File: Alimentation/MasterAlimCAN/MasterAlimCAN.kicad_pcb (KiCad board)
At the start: 2 copper layers, 85 x 111 mm, 95 parts, among them J1 BATT, J10 Alim OUT, J11 ALIM 3 IN, J2 DEBUG, J3 In App Prog, J4 I2C1_5, J5 I2C2_5, J6 CAN1, J7 CAN2, J8 Conn AU, J9 Conn AU, Q1 BSS138, Q2 BSS138, SW1 RESET, SW2 BOOT0, U1 AMS1117-3.3, U10 PTN78020W_EUK-7, U2 STM32G474RETx, U3 74LVC1G02, U4 74LVC1G02, U5 MCP2558FD-xSN, U6 ACS711xEXLT-15AB, U7 ACS711xEXLT-15AB, U8 ACS711xEXLT-15AB, U9 PTN78020W_EUK-7, Y1 16MHz

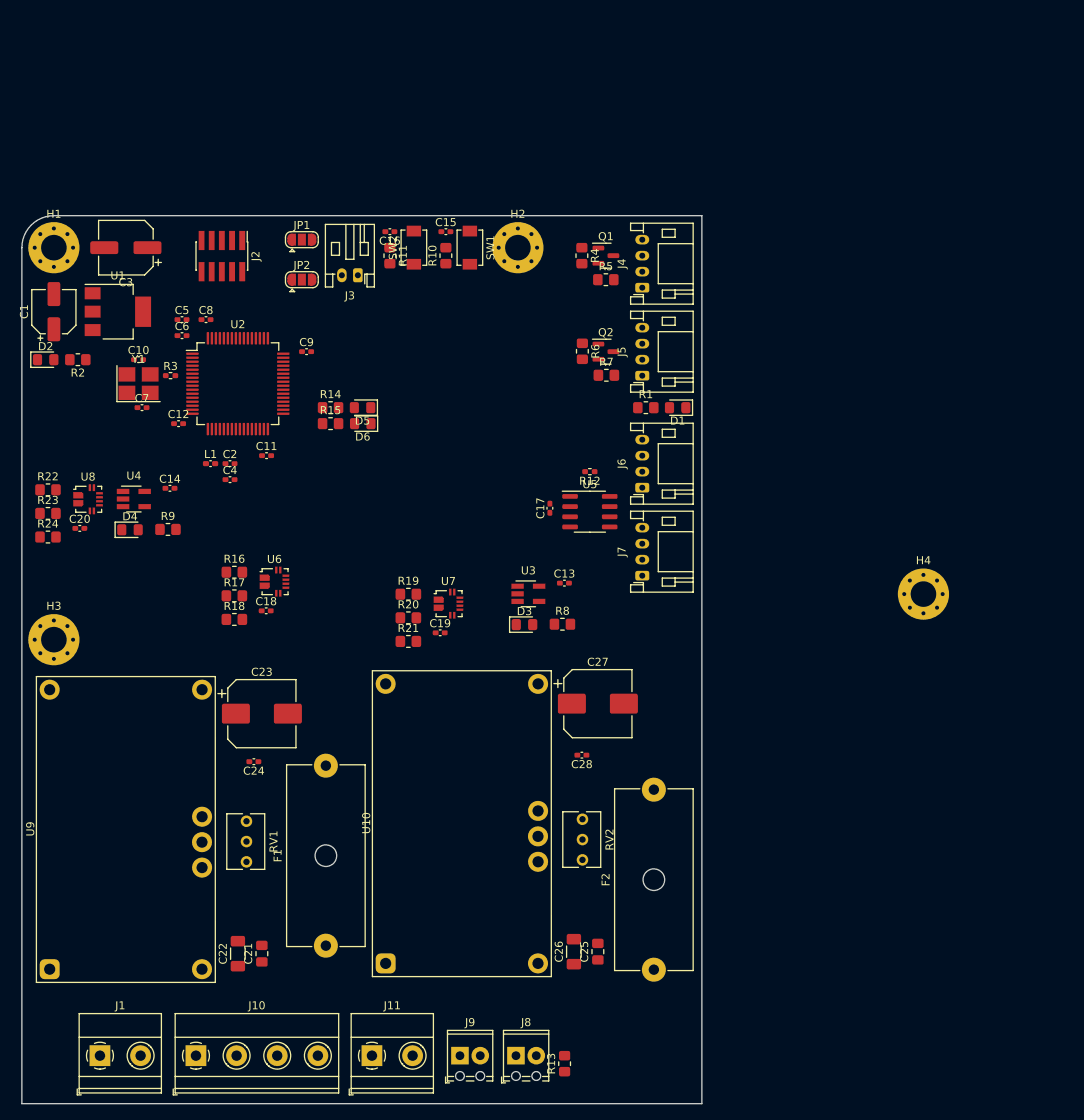
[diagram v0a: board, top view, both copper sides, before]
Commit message: New disposition for alim CAN
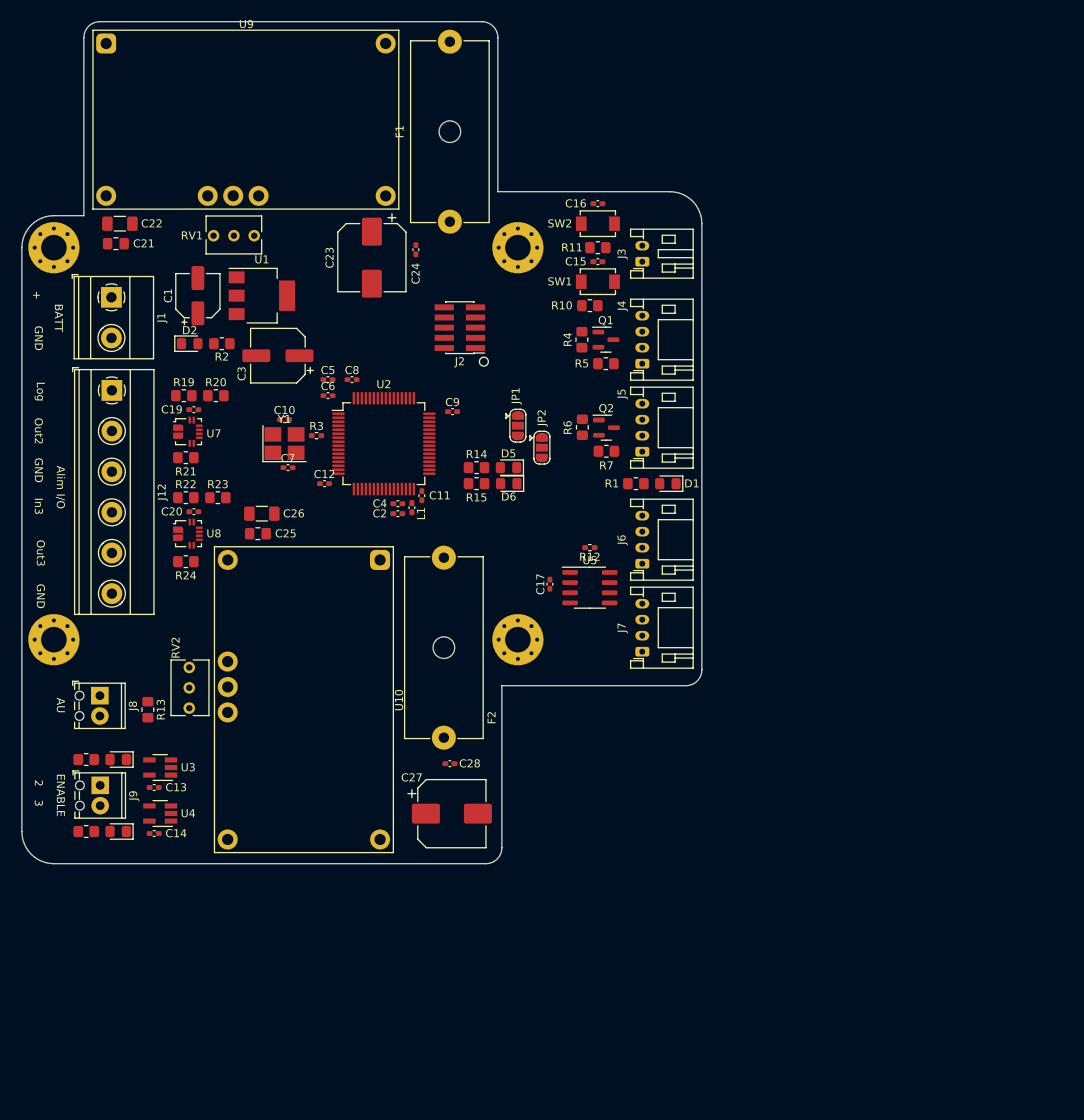
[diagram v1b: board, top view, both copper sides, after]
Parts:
- removed C18: 100n, Capacitor_SMD:C_0402_1005Metric_Pad0.74x0.62mm_HandSolder
- removed J10: Alim OUT, TerminalBlock_Phoenix:TerminalBlock_Phoenix_MKDS-1,5-4-5.08_1x04_P5.08mm_Horizontal
- removed J11: ALIM 3 IN, TerminalBlock_Phoenix:TerminalBlock_Phoenix_MKDS-1,5-2-5.08_1x02_P5.08mm_Horizontal
- removed R16: 5.6k, Resistor_SMD:R_0805_2012Metric_Pad1.20x1.40mm_HandSolder
- removed R17: 1.8k, Resistor_SMD:R_0805_2012Metric_Pad1.20x1.40mm_HandSolder
- removed R18: 10k, Resistor_SMD:R_0805_2012Metric_Pad1.20x1.40mm_HandSolder
- removed U6: ACS711xEXLT-15AB, Sensor_Current:Allegro_QFN-12-10-1EP_3x3mm_P0.5mm
- added J12: Alim I/O, TerminalBlock_Phoenix:TerminalBlock_Phoenix_MKDS-1,5-6-5.08_1x06_P5.08mm_Horizontal, F.Cu at (80.2, 90.8)
- U10, U9: footprint Module:Texas_EUK_R-PDSS-T7_THT -> ARIG:Texas_EUK_R-PDSS-T7_THT
- moved U9 115.9 mm to (79.5, 47.5), turned to 0 degrees
- moved F1 114.1 mm to (122.5, 47.2), turned to -90 degrees
- moved J1 94.8 mm to (80.2, 79.2), turned to -90 degrees
- moved C22 92.4 mm to (81.2, 70.0), turned to 0 degrees
- moved C21 90.6 mm to (80.8, 72.5), turned to 0 degrees
- moved RV1 78.4 mm to (93.0, 71.5), turned to 180 degrees
- moved J8 68.8 mm to (78.8, 129.0), turned to -90 degrees
- moved R13 68.3 mm to (84.8, 130.8), turned to -90 degrees
- moved C25 67.4 mm to (98.5, 108.8), turned to 0 degrees
- moved C26 67.2 mm to (99.0, 106.2), turned to 0 degrees
- moved C24 67.1 mm to (118.2, 73.2), turned to -90 degrees
- moved R8 61.9 mm to (77.0, 137.0)
- moved C23 58.6 mm to (112.8, 74.2), turned to -90 degrees
- moved F2 57.8 mm to (121.8, 111.8), turned to -90 degrees
- moved C13 57.3 mm to (85.5, 140.5)
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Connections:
- F1 pad 1: /Alim 1/ALIM_OUT -> +5V
- U2 pad 11: FAULT_1 -> unconnected-(U2-PC3-Pad11)
- U2 pad 12: ANA_VOLT_1 -> unconnected-(U2-PA0-Pad12)
- U2 pad 13: ANA_CURRENT_1 -> unconnected-(U2-PA1-Pad13)
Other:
- board size 85 x 111 mm -> 85 x 105.2 mm
- board text added: "+"
- board text added: "2"
- board text added: "3"
- board text added: "AU"
- board text added: "Alim I/O"
- board text added: "BATT"
- board text added: "ENABLE"
- board text added: "GND"
- board text added: "In3"
- board text added: "Log"
- board text added: "Out2"
- board text added: "Out3"

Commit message: New placement for Alim
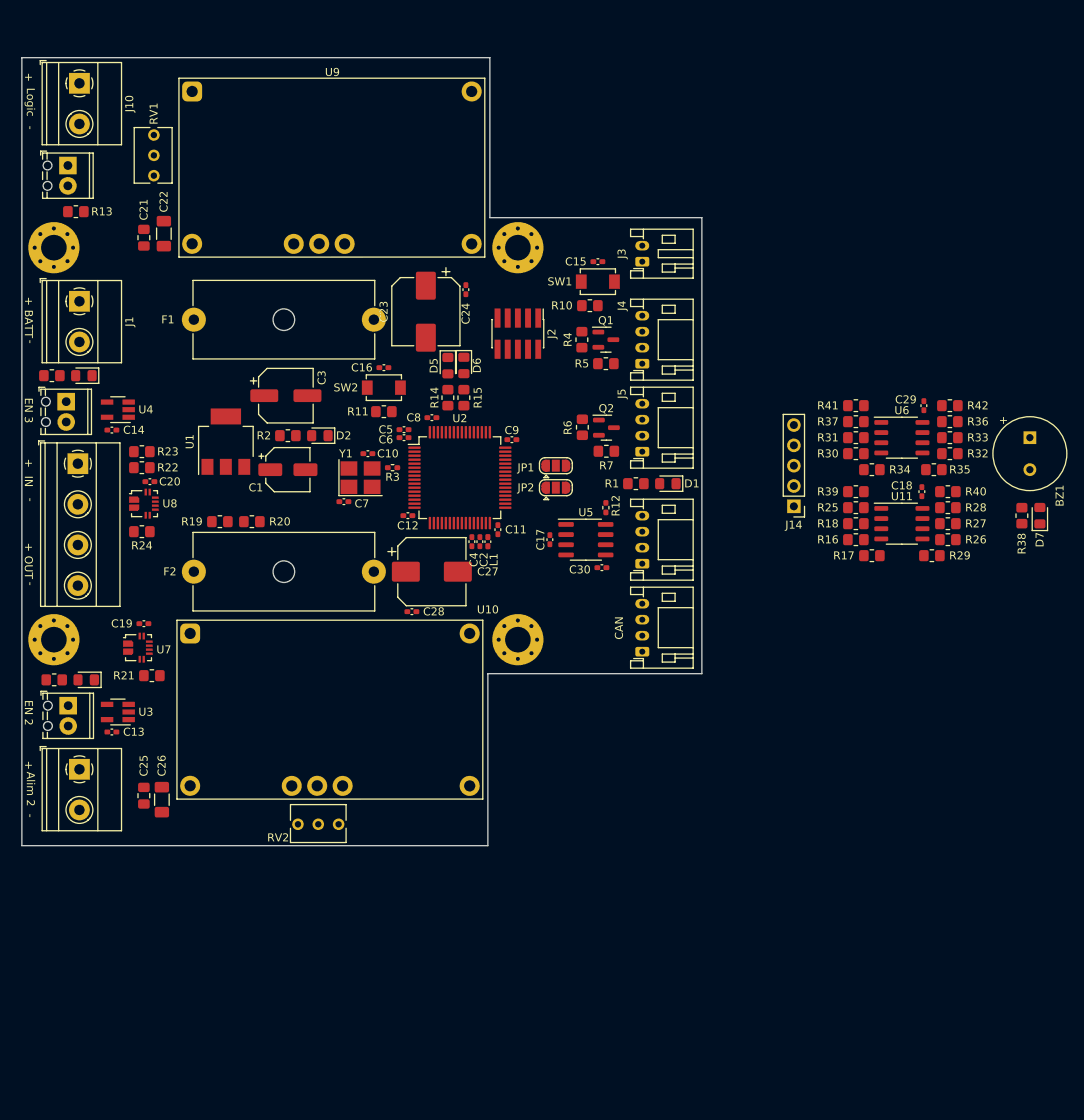
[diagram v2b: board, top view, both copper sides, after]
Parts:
- added BZ1: Buzzer, Buzzer_Beeper:MagneticBuzzer_CUI_CST-931RP-A, F.Cu at (195.0, 96.7)
- added C18: 100n, Capacitor_SMD:C_0402_1005Metric_Pad0.74x0.62mm_HandSolder, F.Cu at (181.5, 103.5)
- added C29: 100n, Capacitor_SMD:C_0402_1005Metric_Pad0.74x0.62mm_HandSolder, F.Cu at (181.8, 92.8)
- added C30: 100n, Capacitor_SMD:C_0402_1005Metric_Pad0.74x0.62mm_HandSolder, F.Cu at (141.5, 113.0)
- added D7: Red, LED_SMD:LED_0805_2012Metric_Pad1.15x1.40mm_HandSolder, F.Cu at (196.2, 106.5)
- added J10: Alim Log, TerminalBlock_Phoenix:TerminalBlock_Phoenix_MKDS-1,5-2-5.08_1x02_P5.08mm_Horizontal, F.Cu at (76.2, 52.5)
- added J11: Alim 2, TerminalBlock_Phoenix:TerminalBlock_Phoenix_MKDS-1,5-2-5.08_1x02_P5.08mm_Horizontal, F.Cu at (76.2, 138.2)
- added J13: Alim 3, TerminalBlock_Phoenix:TerminalBlock_Phoenix_MKDS-1,5-4-5.08_1x04_P5.08mm_Horizontal, F.Cu at (76.0, 100.0)
- added J14: Lipo Cells, Connector_PinHeader_2.54mm:PinHeader_1x05_P2.54mm_Vertical, F.Cu at (165.5, 105.3)
- added R16: 10k, Resistor_SMD:R_0805_2012Metric_Pad1.20x1.40mm_HandSolder, F.Cu at (173.2, 109.5)
- added R17: 7.5k, Resistor_SMD:R_0805_2012Metric_Pad1.20x1.40mm_HandSolder, F.Cu at (175.2, 111.5)
- added R18: 10k, Resistor_SMD:R_0805_2012Metric_Pad1.20x1.40mm_HandSolder, F.Cu at (173.2, 107.5)
- added R25: 7.5k, Resistor_SMD:R_0805_2012Metric_Pad1.20x1.40mm_HandSolder, F.Cu at (173.2, 105.5)
- added R26: 10k, Resistor_SMD:R_0805_2012Metric_Pad1.20x1.40mm_HandSolder, F.Cu at (184.8, 109.5)
- added R27: 10k, Resistor_SMD:R_0805_2012Metric_Pad1.20x1.40mm_HandSolder, F.Cu at (184.8, 107.5)
- added R28: 7.5k, Resistor_SMD:R_0805_2012Metric_Pad1.20x1.40mm_HandSolder, F.Cu at (184.8, 105.5)
- added R29: 7.5k, Resistor_SMD:R_0805_2012Metric_Pad1.20x1.40mm_HandSolder, F.Cu at (182.8, 111.5)
- added R30: 10k, Resistor_SMD:R_0805_2012Metric_Pad1.20x1.40mm_HandSolder, F.Cu at (173.2, 98.8)
- added R31: 10k, Resistor_SMD:R_0805_2012Metric_Pad1.20x1.40mm_HandSolder, F.Cu at (173.2, 96.8)
- added R32: 10k, Resistor_SMD:R_0805_2012Metric_Pad1.20x1.40mm_HandSolder, F.Cu at (185.0, 98.8)
- added R33: 10k, Resistor_SMD:R_0805_2012Metric_Pad1.20x1.40mm_HandSolder, F.Cu at (185.0, 96.8)
- added R34: 7.5k, Resistor_SMD:R_0805_2012Metric_Pad1.20x1.40mm_HandSolder, F.Cu at (175.2, 100.8)
- added R35: 7.5k, Resistor_SMD:R_0805_2012Metric_Pad1.20x1.40mm_HandSolder, F.Cu at (183.0, 100.8)
- added R36: 7.5k, Resistor_SMD:R_0805_2012Metric_Pad1.20x1.40mm_HandSolder, F.Cu at (185.0, 94.8)
- added R37: 7.5k, Resistor_SMD:R_0805_2012Metric_Pad1.20x1.40mm_HandSolder, F.Cu at (173.2, 94.8)
- added R38: 68, Resistor_SMD:R_0805_2012Metric_Pad1.20x1.40mm_HandSolder, F.Cu at (194.0, 106.5)
- added R39: 100k, Resistor_SMD:R_0805_2012Metric_Pad1.20x1.40mm_HandSolder, F.Cu at (173.2, 103.5)
- added R40: 100k, Resistor_SMD:R_0805_2012Metric_Pad1.20x1.40mm_HandSolder, F.Cu at (184.8, 103.5)
- added R41: 100k, Resistor_SMD:R_0805_2012Metric_Pad1.20x1.40mm_HandSolder, F.Cu at (173.2, 92.8)
- added R42: 100k, Resistor_SMD:R_0805_2012Metric_Pad1.20x1.40mm_HandSolder, F.Cu at (185.0, 92.8)
- added U11: LM358, Package_SO:SO-8_3.9x4.9mm_P1.27mm, F.Cu at (179.0, 107.5)
- added U6: LM358, Package_SO:SO-8_3.9x4.9mm_P1.27mm, F.Cu at (179.0, 96.8)
- J12: value Alim I/O -> EN 3; footprint TerminalBlock_Phoenix:TerminalBlock_Phoenix_MKDS-1,5-6-5.08_1x06_P5.08mm_Horizontal -> TerminalBlock_Phoenix:TerminalBlock_Phoenix_MPT-0,5-2-2.54_1x02_P2.54mm_Horizontal
- J9: value Conn AU -> EN 2
- moved J8 66.4 mm to (74.8, 62.7)
- moved R13 62.9 mm to (75.8, 68.5), turned to 180 degrees
- moved D4 57.1 mm to (76.8, 89.0)
- moved R9 57.1 mm to (72.8, 89.0)
- moved U4 50.8 mm to (81.0, 93.2)
- moved C14 50.7 mm to (80.2, 95.8)
- moved F1 47.2 mm to (90.5, 82.0), turned to 0 degrees
- moved C26 37.9 mm to (86.5, 142.0), turned to -90 degrees
- moved C25 35.7 mm to (84.2, 141.5), turned to -90 degrees
- moved C16 33.7 mm to (114.2, 88.0)
- moved R11 33.7 mm to (114.2, 93.5)
- moved SW2 33.7 mm to (114.2, 90.5)
- moved F2 31.3 mm to (90.5, 113.5), turned to 0 degrees
- moved C27 30.4 mm to (120.2, 113.5)
- moved U7 27.7 mm to (83.5, 123.0)
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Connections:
- net +12V renamed +BATT
- J12 pad 1: +5V -> EN_ALIM_3
- J12 pad 2: AlimOut2 -> EN_ALIM_3
- J9 pad 2: EN_ALIM_3 -> EN_ALIM_2
- U2 pad 10: unconnected-(U2-PC2-Pad10) -> ANA_CELL3
- U2 pad 11: unconnected-(U2-PC3-Pad11) -> ANA_CELL4
- U2 pad 12: unconnected-(U2-PA0-Pad12) -> ANA_VOLT_2
- U2 pad 13: unconnected-(U2-PA1-Pad13) -> ANA_CURRENT_2
- U2 pad 14: ANA_VOLT_2 -> ANA_VOLT_3
- U2 pad 17: ANA_CURRENT_2 -> ANA_CURRENT_3
- U2 pad 20: ANA_VOLT_3 -> unconnected-(U2-PA6-Pad20)
- U2 pad 21: ANA_CURRENT_3 -> unconnected-(U2-PA7-Pad21)
- U2 pad 33: AU_KO -> unconnected-(U2-PB11-Pad33)
- U2 pad 35: AU_OK -> unconnected-(U2-PB13-Pad35)
- U2 pad 37: AU -> unconnected-(U2-PB15-Pad37)
- U2 pad 4: unconnected-(U2-PC15-Pad4) -> WARN_BATT
- U2 pad 51: unconnected-(U2-PA15-Pad51) -> BUZZER
- U2 pad 57: unconnected-(U2-PB4-Pad57) -> AU_KO
- U2 pad 58: unconnected-(U2-PB5-Pad58) -> AU_OK
- U2 pad 59: unconnected-(U2-PB6-Pad59) -> AU
- U2 pad 8: unconnected-(U2-PC0-Pad8) -> ANA_CELL1
- U2 pad 9: unconnected-(U2-PC1-Pad9) -> ANA_CELL2
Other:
- board size 85 x 105.2 mm -> 85 x 98.5 mm
- board text added: "-"
- board text added: "Alim 2"
- board text added: "CAN"
- board text added: "EN 2"
- board text added: "EN 3"
- board text added: "IN"
- board text added: "Logic"
- board text added: "OUT"
- board text removed: "2"
- board text removed: "3"
- board text removed: "AU"
- board text removed: "Alim I/O"
- board text removed: "ENABLE"
- board text removed: "GND"
- board text removed: "In3"
- board text removed: "Log"
- board text removed: "Out2"
- board text removed: "Out3"

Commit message: Finish component placement on MasterAlimCAN
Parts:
- removed J14: Lipo Cells, Connector_PinHeader_2.54mm:PinHeader_1x05_P2.54mm_Vertical
- added J15: Lipo Cells, Connector_JST:JST_PH_S5B-PH-K_1x05_P2.00mm_Horizontal, F.Cu at (140.8, 140.0)
- moved D7 71.2 mm to (137.5, 66.2), turned to -90 degrees
- moved R38 67.6 mm to (139.8, 66.2), turned to -90 degrees
- moved BZ1 56.0 mm to (148.0, 66.2), turned to -90 degrees
- moved R11 47.6 mm to (141.5, 54.5), turned to 90 degrees
- moved C16 44.0 mm to (139.5, 52.0), turned to 0 degrees
- moved SW2 42.7 mm to (137.2, 54.5)
- moved C29 42.7 mm to (147.5, 118.2)
- moved R30 42.7 mm to (139.0, 124.2)
- moved R31 42.7 mm to (139.0, 122.2)
- moved R32 42.7 mm to (150.8, 124.2)
- moved R33 42.7 mm to (150.8, 122.2)
- moved R34 42.7 mm to (141.0, 126.2)
- moved R35 42.7 mm to (148.8, 126.2)
- moved R36 42.7 mm to (150.8, 120.2)
- moved R37 42.7 mm to (139.0, 120.2)
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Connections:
- U2 pad 10: ANA_CELL3 -> ANA_CELL2
- U2 pad 11: ANA_CELL4 -> ANA_CELL1
- U2 pad 8: ANA_CELL1 -> ANA_CELL4
- U2 pad 9: ANA_CELL2 -> ANA_CELL3
- U5 pad 6: Net-(J6-Pin_3) -> Net-(J6-Pin_2)
- U5 pad 7: Net-(J6-Pin_2) -> Net-(J6-Pin_3)
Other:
- outline, holes or cut-outs redrawn
- board text added: "I2C"
- board text added: "In App Prog"
- board text added: "PWR"
